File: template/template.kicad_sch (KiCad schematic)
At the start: 4 parts, among them SW1 MHPS2285

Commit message: Added schema and BoM
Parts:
- R1: value R -> 90
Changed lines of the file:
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@@
+			)
+		)
+		(property "Manufacturer No." "C5SMF-RJE-CT0W0BB1"
+			(at 157.48 101.6 0)
+			(effects
+				(font
+					(size 1.27 1.27)
+				)
+				(hide yes)
 			)
 		)
@@
 		)
 		(property "Mouser No." "941-C5SMFRJECT0W0BB1"
-			(at 157.48 101.6 0)
-			(effects
-				(font
-					(size 1.27 1.27)
-				)
-				(hide yes)
-			)
-		)
-		(property "Manufacturer No." "C5SMF-RJE-CT0W0BB1"
 			(at 157.48 101.6 0)
 			(effects
@@
 			)
 		)
-		(property "Value" "R"
+		(property "Value" "90"
 			(at 159.512 95.25 0)
 			(effects

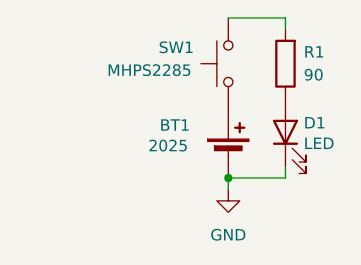
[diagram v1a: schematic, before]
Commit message: Added more correct battery symbol
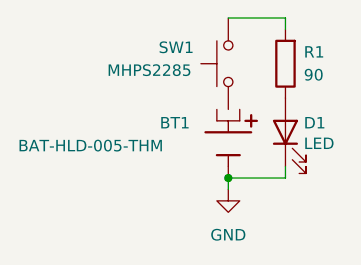
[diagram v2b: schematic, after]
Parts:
- removed BT1: 2025, symbol Device:Battery_Cell
- added BT1: BAT-HLD-005-THM, -Robot Uprising:BAT-HLD-005-THM, symbol -Robot Uprising:BAT-HLD-005-THM
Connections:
- net GND: now also BT1.
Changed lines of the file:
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@@
+	)
+	(symbol
+		(lib_id "-Robot Uprising:BAT-HLD-005-THM")
+		(at 151.13 102.87 270)
+		(unit 1)
+		(exclude_from_sim no)
+		(in_bom yes)
+		(on_board yes)
+		(dnp no)
+		(property "Reference" "BT1"
+			(at 143.51 100.584 90)
+			(effects
+				(font
+					(size 1.27 1.27)
+				)
+				(justify left)
+			)
+		)
+		(property "Value" "BAT-HLD-005-THM"
+			(at 127.762 103.124 90)
+			(effects
+				(font
+					(size 1.27 1.27)
+				)
+				(justify left)
+			)
+		)
+		(property "Footprint" "-Robot Uprising:BAT-HLD-005-THM"
+			(at 158.496 103.124 0)
+			(effects
+				(font
+					(size 1.27 1.27)
+				)
+				(justify bottom)
+				(hide yes)
+			)
+		)
+		(property "Datasheet" ""
+			(at 151.13 102.87 0)
+			(effects
+				(font
+					(size 1.27 1.27)
+				)
+				(hide yes)
+			)
+		)
+		(property "Description" ""
+			(at 151.13 102.87 0)
+			(effects
+				(font
+					(size 1.27 1.27)
+				)
+				(hide yes)
+			)
+		)
+		(property "SnapEDA_Link" "https://www.snapeda.com/parts/BAT-HLD-005-THM/Linx/view-part/?ref=snap"
+			(at 154.178 103.124 0)
+			(effects
+				(font
+					(size 1.27 1.27)
+				)
+				(justify bottom)
+				(hide yes)
+			)
+		)
+		(property "Check_prices" "https://www.snapeda.com/parts/BAT-HLD-005-THM/Linx/view-part/?ref=eda"
+			(at 137.414 101.854 0)
+			(effects
+				(font
+					(size 1.27 1.27)
+				)
+				(justify bottom)
+				(hide yes)
+			)
+		)
+		(property "Package" "None"
+			(at 141.478 102.87 0)
+			(effects
+				(font
+					(size 1.27 1.27)
+				)
+				(justify bottom)
+				(hide yes)
+			)
+		)
+		(property "Price" "None"
+			(at 143.51 102.616 0)
+			(effects
+				(font
+					(size 1.27 1.27)
+				)
+				(justify bottom)
+				(hide yes)
+			)
+		)
+		(property "MF" "Linx Technologies Inc."
+			(at 139.7 102.87 0)
+			(effects
+				(font
+					(size 1.27 1.27)
+				)
+				(justify bottom)
+				(hide yes)
+			)
+		)
+		(property "MP" "BAT-HLD-005-THM"
+			(at 136.144 103.124 0)
+			(effects
+				(font
+					(size 1.27 1.27)
+				)
+				(justify bottom)
+				(hide yes)
+			)
+		)
+		(property "Purchase-URL" "https://www.snapeda.com/api/url_track_click_mouser/?unipart_id=6305472&manufacturer=Linx Technologies Inc.&part_name=BAT-HLD-005-THM&search_term=None"
+			(at 162.56 102.87 0)
+			(effects
+				(font
+					(size 1.27 1.27)
+				)
+				(justify bottom)
+				(hide yes)
+			)
+		)
+		(property "Availability" "In Stock"
+			(at 133.604 102.87 0)
+			(effects
+				(font
+					(size 1.27 1.27)
+				)
+				(justify bottom)
+				(hide yes)
+			)
+		)
+		(property "Description_1" "Battery Holder Coin 20 THM Nickel"
+			(at 156.464 102.87 0)
+			(effects
+				(font
+					(size 1.27 1.27)
+				)
+				(justify bottom)
+				(hide yes)
+			)
+		)
+		(pin ""
+		)
+		(pin ""
+		)
+		(pin ""
+		)
+		(instances
+			(project ""
+				(path "/5dc43014-3e3d-4f52-b93f-2dd7b4be6a5c"
+					(reference "BT1")
+					(unit 1)
+				)
+			)
+		)
 	)
 	(symbol
@@
 					(unit 1)
 				)
-			)
-		)
-	)
-	(symbol
-		(lib_id "Device:Battery_Cell")
-		(at 151.13 104.14 0)
-		(unit 1)
-		(exclude_from_sim no)
-		(in_bom yes)
-		(on_board yes)
-		(dnp no)
-		(property "Reference" "BT1"
-			(at 143.51 100.838 0)
-			(effects
-				(font
-					(size 1.27 1.27)
-				)
-				(justify left)
-			)
-		)
-		(property "Value" "2025"
-			(at 142.24 103.124 0)
-			(effects
-				(font
-					(size 1.27 1.27)
-				)
-				(justify left)
-			)
-		)
-		(property "Footprint" ""
-			(at 151.13 102.616 90)
-			(effects
-				(font
-					(size 1.27 1.27)
-				)
-				(hide yes)
-			)
-		)
-		(property "Datasheet" "kicad-embed://BAT-HLD-005-THM.pdf"
-			(at 151.13 102.616 90)
-			(effects
-				(font
-					(size 1.27 1.27)
-				)
-				(hide yes)
-			)
-		)
-		(property "Description" "Single-cell battery"
-			(at 151.13 104.14 0)
-			(effects
-				(font
-					(size 1.27 1.27)
-				)
-				(hide yes)
-			)
-		)
-		(property "Manufacturer No." "BAT-HLD-005-THM"
-			(at 151.13 104.14 0)
-			(effects
-				(font
-					(size 1.27 1.27)
-				)
-				(hide yes)
-			)
-		)
-		(property "Mouser Link" "https://www.mouser.fi/ProductDetail/TE-Connectivity-Linx-Technologies/BAT-HLD-005-THM?qs=TuK3vfAjtkXjhh4FQtEXIQ%3D%3D"
-			(at 151.13 104.14 0)
-			(effects
-				(font
-					(size 1.27 1.27)
-				)
-				(hide yes)
-			)
-		)
-		(property "Mouser No." "712-BAT-HLD-005-THM"
-			(at 151.13 104.14 0)
-			(effects
-				(font
-					(size 1.27 1.27)
-				)
-				(hide yes)
-			)
-		)
-		(pin "2"
-		)
-		(pin "1"
-		)
-		(instances
-			(project ""
-				(path "/5dc43014-3e3d-4f52-b93f-2dd7b4be6a5c"
-					(reference "BT1")
-					(unit 1)
-				)

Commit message: Batter working
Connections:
- net GND: now also BT1.N; no longer BT1.
- net at SW1.1: now also BT1.P1, BT1.P2
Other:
- moved on the sheet: SW1
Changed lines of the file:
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@@
+	)
+	(junction
+		(at 151.13 99.06)
+		(diameter 0)
+		(color 0 0 0 0)
 	)
 	(junction
@@
 	(wire
 		(pts
-			(xy 157.48 88.9) (xy 151.13 88.9)
+			(xy 157.48 86.36) (xy 151.13 86.36)
+		)
+		(stroke
+			(width 0)
+			(type default)
+		)
+	)
+	(wire
+		(pts
+			(xy 151.13 99.06) (xy 152.4 99.06)
 		)
 		(stroke
@@
 	(wire
 		(pts
-			(xy 157.48 88.9) (xy 157.48 90.17)
+			(xy 157.48 86.36) (xy 157.48 90.17)
 		)
 		(stroke
@@
 		(pts
 			(xy 157.48 105.41) (xy 157.48 106.68)
+		)
+		(stroke
+			(width 0)
+			(type default)
+		)
+	)
+	(wire
+		(pts
+			(xy 149.86 99.06) (xy 151.13 99.06)
+		)
+		(stroke
+			(width 0)
+			(type default)
+		)
+	)
+	(wire
+		(pts
+			(xy 151.13 96.52) (xy 151.13 99.06)
 		)
 		(stroke
@@
 	(symbol
 		(lib_id "-Robot Uprising:BAT-HLD-005-THM")
-		(at 151.13 102.87 270)
+		(at 151.13 104.14 270)
 		(unit 1)
 		(exclude_from_sim no)
@@
 		(dnp no)
 		(property "Reference" "BT1"
-			(at 143.51 100.584 90)
+			(at 143.51 101.854 90)
 			(effects
 				(font
@@
 		)
 		(property "Value" "BAT-HLD-005-THM"
-			(at 127.762 103.124 90)
+			(at 127.762 104.394 90)
 			(effects
 				(font
@@
 		)
 		(property "Footprint" "-Robot Uprising:BAT-HLD-005-THM"
-			(at 158.496 103.124 0)
+			(at 158.496 104.394 0)
 			(effects
 				(font
@@
 		)
 		(property "Datasheet" ""
-			(at 151.13 102.87 0)
+			(at 151.13 104.14 0)
 			(effects
 				(font
@@
 		)
 		(property "Description" ""
-			(at 151.13 102.87 0)
+			(at 151.13 104.14 0)
 			(effects
 				(font
@@
 		)
 		(property "SnapEDA_Link" "https://www.snapeda.com/parts/BAT-HLD-005-THM/Linx/view-part/?ref=snap"
-			(at 154.178 103.124 0)
+			(at 154.178 104.394 0)
 			(effects
 				(font
@@
 		)
 		(property "Check_prices" "https://www.snapeda.com/parts/BAT-HLD-005-THM/Linx/view-part/?ref=eda"
-			(at 137.414 101.854 0)
+			(at 137.414 103.124 0)
 			(effects
 				(font
@@
 		)
 		(property "Package" "None"
-			(at 141.478 102.87 0)
+			(at 141.478 104.14 0)
 			(effects
 				(font
@@
 		)
 		(property "Price" "None"
-			(at 143.51 102.616 0)
+			(at 143.51 103.886 0)
 			(effects
 				(font
@@
 		)
 		(property "MF" "Linx Technologies Inc."
-			(at 139.7 102.87 0)
+			(at 139.7 104.14 0)
 			(effects
 				(font
@@
 		)
 		(property "MP" "BAT-HLD-005-THM"
-			(at 136.144 103.124 0)
+			(at 136.144 104.394 0)
 			(effects
 				(font
@@
 		)
 		(property "Purchase-URL" "https://www.snapeda.com/api/url_track_click_mouser/?unipart_id=6305472&manufacturer=Linx Technologies Inc.&part_name=BAT-HLD-005-THM&search_term=None"
-			(at 162.56 102.87 0)
+			(at 162.56 104.14 0)
 			(effects
 				(font
@@
 		)
 		(property "Availability" "In Stock"
-			(at 133.604 102.87 0)
+			(at 133.604 104.14 0)
 			(effects
 				(font
@@
 		)
 		(property "Description_1" "Battery Holder Coin 20 THM Nickel"
-			(at 156.464 102.87 0)
-			(effects
-				(font
-					(size 1.27 1.27)
-				)
-				(justify bottom)
-				(hide yes)
-			)
-		)
-		(pin ""
-		)
-		(pin ""
-		)
-		(pin ""
+			(at 156.464 104.14 0)
+			(effects
+				(font
+					(size 1.27 1.27)
+				)
+				(justify bottom)
+				(hide yes)
+			)
+		)
+		(pin "N"
+		)
+		(pin "P1"
+		)
+		(pin "P2"
 		)
 		(instances
@@
 	(symbol
 		(lib_id "Switch:SW_Push")
-		(at 151.13 93.98 90)
+		(at 151.13 91.44 90)
 		(unit 1)
 		(exclude_from_sim no)
@@
 		(dnp no)
 		(property "Reference" "SW1"
-			(at 147.32 92.202 90)
+			(at 147.32 89.662 90)
 			(effects
 				(font
@@
 		)
 		(property "Value" "MHPS2285"
-			(at 147.066 94.742 90)
+			(at 147.066 92.202 90)
 			(effects
 				(font
@@
 		)
 		(property "Footprint" ""
-			(at 146.05 93.98 0)
+			(at 146.05 91.44 0)
 			(effects
 				(font
@@
 		)
 		(property "Datasheet" "kicad-embed://MHPS2285V.pdf"
-			(at 146.05 93.98 0)
+			(at 146.05 91.44 0)
 			(effects
 				(font
@@
 		)
 		(property "Description" "Push button switch, generic, two pins"
-			(at 151.13 93.98 0)
+			(at 151.13 91.44 0)
 			(effects
 				(font
@@
 		)
 		(property "Manufacturer No." "MHPS2285V"
-			(at 151.13 93.98 90)
+			(at 151.13 91.44 90)
 			(effects
 				(font
@@
 		)
 		(property "Mouser Link" "https://www.mouser.fi/ProductDetail/Apem/MHPS2285V?qs=6hR9CYnVCPAFDBxI9FF22g%3D%3D"
-			(at 151.13 93.98 90)
+			(at 151.13 91.44 90)
 			(effects
 				(font
@@
 		)
 		(property "Mouser No." " 642-MHPS2285V "
-			(at 151.13 93.98 90)
-			(effects
-				(font
+			(at 151.13 91.44 90)
+			(effects
+				(font

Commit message: Template ready
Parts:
- removed SW1: MHPS2285, symbol Switch:SW_Push
- added D2: LED, LED_THT:LED_D5.0mm, symbol Device:LED
- added R2: 47, Resistor_THT:R_Axial_DIN0309_L9.0mm_D3.2mm_P15.24mm_Horizontal, symbol Device:R
- added S1: TS02-66-70-BK-160-LCR-D, Robot Uprising:SW_TS02-66-70-BK-160-LCR-D, symbol Robot Uprising:TS02-66-70-BK-160-LCR-D
- BT1: footprint -Robot Uprising:BAT-HLD-005-THM -> Robot Uprising:BAT-HLD-005-THM
- R1: value 90 -> 47; footprint (none) -> Resistor_THT:R_Axial_DIN0309_L9.0mm_D3.2mm_P15.24mm_Horizontal
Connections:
- net at BT1.P1, BT1.P2: now also S1.3, S1.4
- net at R1.2: now also S1.1, S1.2
- new net: D2.2 (A), R2.1
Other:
- note added: "If you want more LEDs connect this to the circuit. If not remove this."
- note added: "V_bat = 3V V_led = 2.1 V I_led = 10-30 mA R = (3V-2.1V)/10 mA = 90 -> 100 Ohm R = (3V-2.1V)/20 mA = 45 -> 47 Ohm These are different for example different colour or different model"
- moved on the sheet: BT1

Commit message: Cleanup
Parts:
- removed BT1: BAT-HLD-005-THM, Robot Uprising:BAT-HLD-005-THM, symbol -Robot Uprising:BAT-HLD-005-THM
- removed D1: LED, LED_THT:LED_D5.0mm, symbol Device:LED
- removed S1: TS02-66-70-BK-160-LCR-D, Robot Uprising:SW_TS02-66-70-BK-160-LCR-D, symbol Robot Uprising:TS02-66-70-BK-160-LCR-D
- added BT1: BAT-HLD-005-THM, Robot Uprising:BT_BAT-HLD-005-THM, symbol Robot Uprising:BT_BAT-HLD-005-THM
- added D1: LED, LED_THT:LED_D5.0mm, symbol Robot Uprising:D_LED_C5SMF-RJE-CT0W0BB1
- added S1: TS02-66-70-BK-160-LCR-D, Robot Uprising:S_TS02-66-70-BK-160-LCR-D, symbol Robot Uprising:S_TS02-66-70-BK-160-LCR-D
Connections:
- net GND: now also BT1.N, D1.1 (K)
- net at R1.1: now also D1.2 (A)
- net at R1.2: now also S1.1, S1.2
- new net: BT1.P1, BT1.P2, S1.3, S1.4

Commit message: ready
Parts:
- removed D2: LED, LED_THT:LED_D5.0mm, symbol Device:LED
- added D2: LED, LED_THT:LED_D5.0mm, symbol Robot Uprising:D_LED_C5SMF-RJE-CT0W0BB1
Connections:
- net at R2.1: now also D2.2 (A)
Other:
- note added: "If you want more LEDs connect this to the circuit. If not, remove this."
- note removed: "If you want more LEDs connect this to the circuit. If not remove this."
